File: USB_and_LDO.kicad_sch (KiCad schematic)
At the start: 12 parts, among them J2 USB_C_Receptacle_USB2.0_16P, U2 USBLC6-2SC6, U3 MCP1755S

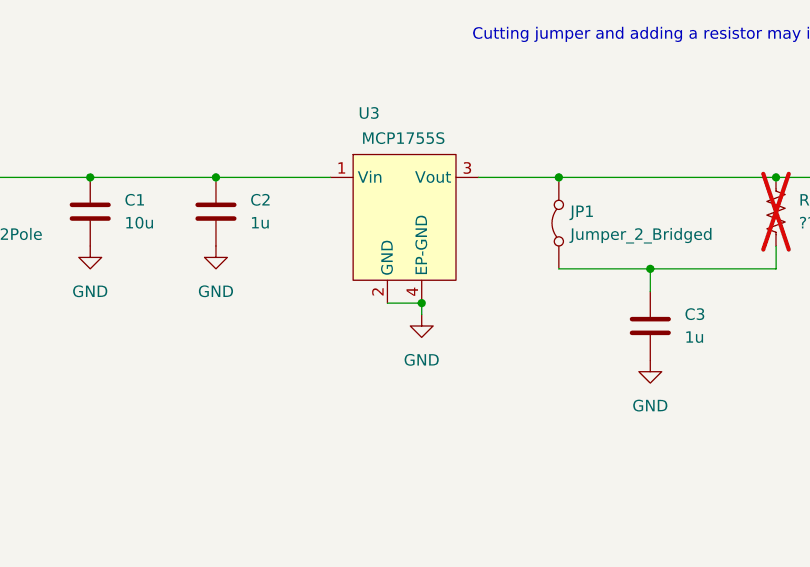
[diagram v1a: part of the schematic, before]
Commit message: Added all footprints
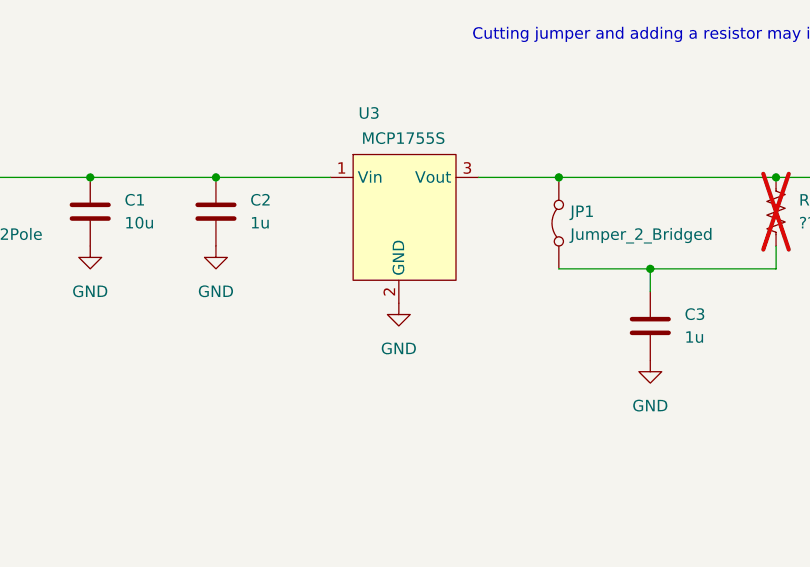
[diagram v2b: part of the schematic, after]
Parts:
- C1, C2, C3: footprint (none) -> Capacitor_SMD:C_1206_3216Metric_Pad1.33x1.80mm_HandSolder
- J2: footprint (none) -> Connector_USB:USB_C_Receptacle_GCT_USB4085
- JP1: footprint (none) -> Jumper:SolderJumper-2_P1.3mm_Bridged_RoundedPad1.0x1.5mm
- R1, R2, R3: footprint (none) -> Resistor_SMD:R_1206_3216Metric_Pad1.30x1.75mm_HandSolder
- TP1, TP2: footprint (none) -> TestPoint:TestPoint_2Pads_Pitch2.54mm_Drill0.8mm
- U3: footprint (none) -> Package_TO_SOT_SMD:SOT-223-3_TabPin2
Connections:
- net GND: no longer U3.4 (EP-GND)
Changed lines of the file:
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@@
-	)
-	(junction
-		(at 190.5 102.87)
-		(diameter 0)
-		(color 0 0 0 0)
 	)
 	(junction
@@
 	(wire
 		(pts
-			(xy 186.69 102.87) (xy 190.5 102.87)
-		)
-		(stroke
-			(width 0)
-			(type default)
-		)
-	)
-	(wire
-		(pts
-			(xy 190.5 102.87) (xy 190.5 104.14)
-		)
-		(stroke
-			(width 0)
-			(type default)
-		)
-	)
-	(wire
-		(pts
 			(xy 59.69 78.74) (xy 59.69 81.28)
 		)
@@
 	(symbol
 		(lib_id "power:GND")
-		(at 190.5 104.14 0)
+		(at 187.96 102.87 0)
 		(unit 1)
 		(exclude_from_sim no)
@@
 		(fields_autoplaced yes)
 		(property "Reference" "#PWR014"
-			(at 190.5 110.49 0)
+			(at 187.96 109.22 0)
 			(effects
 				(font
@@
 		)
 		(property "Value" "GND"
-			(at 190.5 109.22 0)
+			(at 187.96 107.95 0)
 			(effects
 				(font
@@
 		)
 		(property "Footprint" ""
-			(at 190.5 104.14 0)
+			(at 187.96 102.87 0)
 			(effects
 				(font
@@
 		)
 		(property "Datasheet" ""
-			(at 190.5 104.14 0)
+			(at 187.96 102.87 0)
 			(effects
 				(font
@@
 		)
 		(property "Description" "Power symbol creates a global label with name \"GND\" , ground"
-			(at 190.5 104.14 0)
+			(at 187.96 102.87 0)
 			(effects
 				(font
@@
 			)
 		)
-		(property "Footprint" ""
+		(property "Footprint" "Package_TO_SOT_SMD:SOT-223-3_TabPin2"
 			(at 187.96 92.71 0)
 			(effects
@@
 		(pin "2"
 		)
-		(pin "4"
-		)
 		(instances
 			(project "STM32F0-32pin-USBC"
@@
 			)
 		)
-		(property "Footprint" ""
+		(property "Footprint" "Resistor_SMD:R_1206_3216Metric_Pad1.30x1.75mm_HandSolder"
 			(at 50.546 133.604 90)
 			(effects
@@
 			)
 		)
-		(property "Footprint" ""
+		(property "Footprint" "Jumper:SolderJumper-2_P1.3mm_Bridged_RoundedPad1.0x1.5mm"
 			(at 205.74 93.98 0)
 			(effects
@@
 			)
 		)
-		(property "Footprint" ""
+		(property "Footprint" "TestPoint:TestPoint_2Pads_Pitch2.54mm_Drill0.8mm"
 			(at 132.08 93.98 0)
 			(effects
@@
 			)
 		)
-		(property "Footprint" ""
+		(property "Footprint" "Resistor_SMD:R_1206_3216Metric_Pad1.30x1.75mm_HandSolder"
 			(at 230.886 92.964 90)
 			(effects
@@
 			)
 		)
-		(property "Footprint" ""
+		(property "Footprint" "Resistor_SMD:R_1206_3216Metric_Pad1.30x1.75mm_HandSolder"
 			(at 35.306 133.604 90)
 			(effects
@@
 			)
 		)
-		(property "Footprint" ""
+		(property "Footprint" "Capacitor_SMD:C_1206_3216Metric_Pad1.33x1.80mm_HandSolder"
 			(at 168.6052 96.52 0)
 			(effects
@@
 			)
 		)
-		(property "Footprint" ""
+		(property "Footprint" "Capacitor_SMD:C_1206_3216Metric_Pad1.33x1.80mm_HandSolder"
 			(at 216.8652 109.22 0)
 			(effects
@@
 			)
 		)
-		(property "Footprint" ""
+		(property "Footprint" "TestPoint:TestPoint_2Pads_Pitch2.54mm_Drill0.8mm"
 			(at 241.3 93.98 0)
 			(effects
@@
 			)
 		)
-		(property "Footprint" ""
+		(property "Footprint" "Capacitor_SMD:C_1206_3216Metric_Pad1.33x1.80mm_HandSolder"
 			(at 154.6352 96.52 0)
 			(effects
@@
 			)
 		)
-		(property "Footprint" ""
+		(property "Footprint" "Connector_USB:USB_C_Receptacle_GCT_USB4085"
 			(at 48.26 81.28 0)
 			(effects

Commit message: finished part nubers in BOM
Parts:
- C1: MFR (none) -> Kemet; MFR Part No (none) -> C1206C106K4RACTU
- C2, C3: MFR (none) -> Kemet; MFR Part No (none) -> C1206C105K4RACTU
- J2: MFR (none) -> GCT; MFR Part No (none) -> USB4085-GF-A
- R1, R2: MFR (none) -> Vishay; MFR Part No (none) -> CRCW12065K10FKEA
- U2: MFR (none) -> STMicroelectronics; MFR Part No (none) -> USBLC6-2SC6
- U3: MFR (none) -> Microchip; MFR Part No (none) -> MCP1755S-3302E/DB
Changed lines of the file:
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@@
 			)
 		)
-		(property "MFR" ""
+		(property "MFR" "Microchip"
 			(at 187.96 92.71 0)
 			(effects
@@
 			)
 		)
-		(property "MFR Part No" ""
+		(property "MFR Part No" "MCP1755S-3302E/DB"
 			(at 187.96 92.71 0)
 			(effects
@@
 			)
 		)
-		(property "MFR" ""
+		(property "MFR" "STMicroelectronics"
 			(at 77.47 81.28 0)
 			(effects
@@
 			)
 		)
-		(property "MFR Part No" ""
+		(property "MFR Part No" "USBLC6-2SC6"
 			(at 77.47 81.28 0)
 			(effects
@@
 			)
 		)
-		(property "MFR" ""
+		(property "MFR" "Vishay"
 			(at 49.53 133.35 0)
 			(effects
@@
 			)
 		)
-		(property "MFR Part No" ""
+		(property "MFR Part No" "CRCW12065K10FKEA"
 			(at 49.53 133.35 0)
 			(effects
@@
 			)
 		)
-		(property "MFR" ""
+		(property "MFR" "Vishay"
 			(at 34.29 133.35 0)
 			(effects
@@
 			)
 		)
-		(property "MFR Part No" ""
+		(property "MFR Part No" "CRCW12065K10FKEA"
 			(at 34.29 133.35 0)
 			(effects
@@
 			)
 		)
-		(property "MFR" ""
+		(property "MFR" "Kemet"
 			(at 167.64 92.71 0)
 			(effects
@@
 			)
 		)
-		(property "MFR Part No" ""
+		(property "MFR Part No" "C1206C105K4RACTU"
 			(at 167.64 92.71 0)
 			(effects
@@
 			)
 		)
-		(property "MFR" ""
+		(property "MFR" "Kemet"
 			(at 215.9 105.41 0)
 			(effects
@@
 			)
 		)
-		(property "MFR Part No" ""
+		(property "MFR Part No" "C1206C105K4RACTU"
 			(at 215.9 105.41 0)
 			(effects
@@
 			)
 		)
-		(property "MFR" ""
+		(property "MFR" "Kemet"
 			(at 153.67 92.71 0)
 			(effects
@@
 			)
 		)
-		(property "MFR Part No" ""
+		(property "MFR Part No" "C1206C106K4RACTU"
 			(at 153.67 92.71 0)
 			(effects
@@
 			)
 		)
-		(property "MFR" ""
+		(property "MFR" "GCT"
 			(at 44.45 81.28 0)
 			(effects
@@
 			)
 		)
-		(property "MFR Part No" ""
+		(property "MFR Part No" "USB4085-GF-A"
 			(at 44.45 81.28 0)
 			(effects

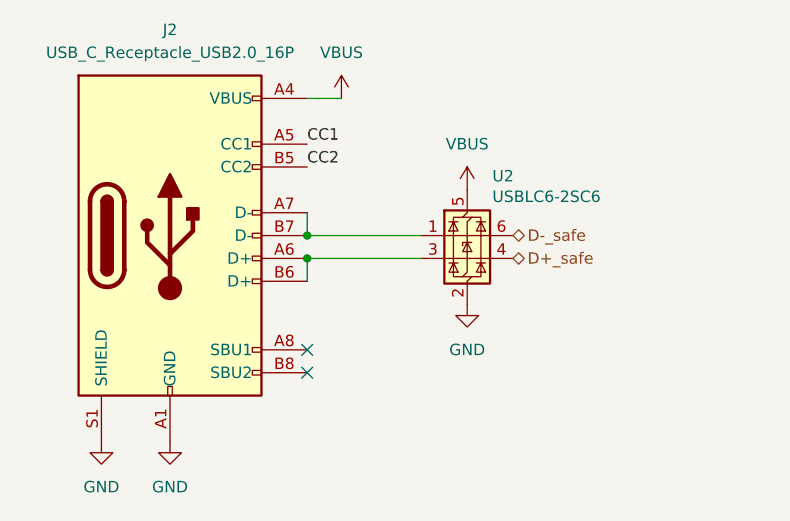
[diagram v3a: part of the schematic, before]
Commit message: preliminary footprint placement
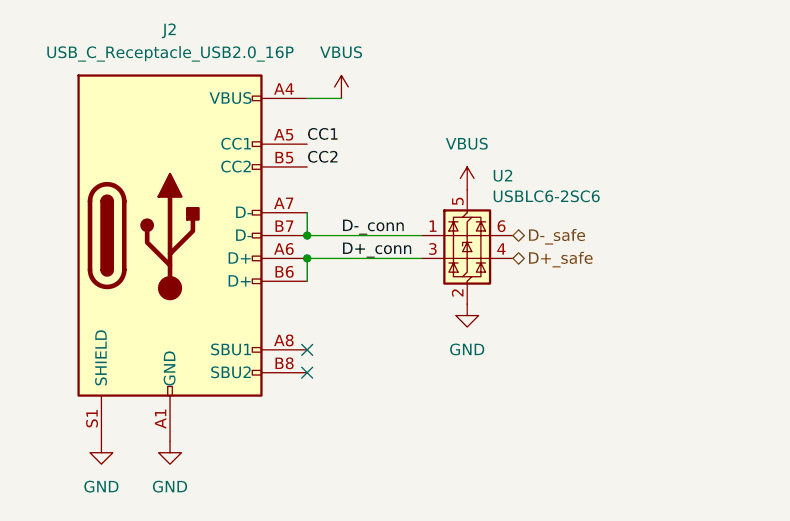
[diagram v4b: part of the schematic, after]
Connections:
- net D-_conn: now reaches J2.A7 (D-), J2.B7 (D-), U2.1 (I/O1)
- net D+_conn: now reaches J2.A6 (D+), J2.B6 (D+), U2.3 (I/O2)
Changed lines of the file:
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@@
+		)
+	)
+	(label "D+_conn"
+		(at 63.5 83.82 0)
+		(fields_autoplaced yes)
+		(effects
+			(font
+				(size 1.27 1.27)
+			)
+			(justify left bottom)
+		)
+	)
+	(label "D-_conn"
+		(at 63.5 81.28 0)
+		(fields_autoplaced yes)
+		(effects
+			(font
+				(size 1.27 1.27)
+			)
+			(justify left bottom)
 		)
 	)

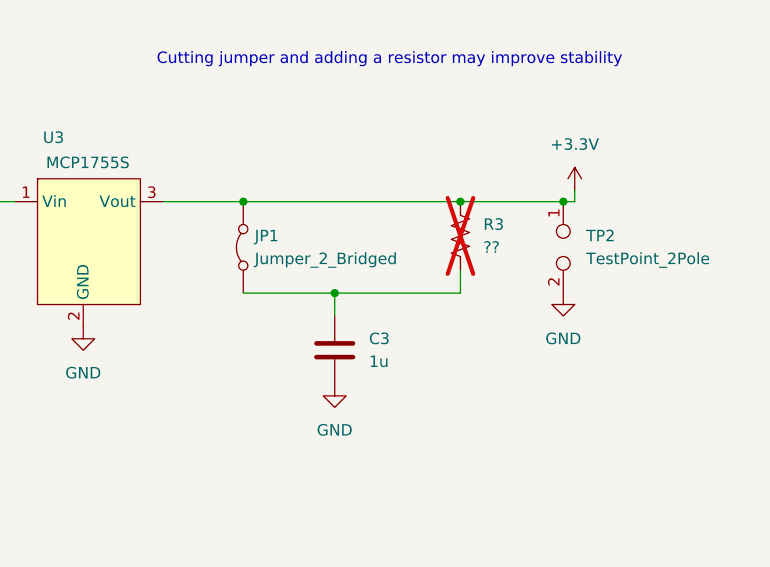
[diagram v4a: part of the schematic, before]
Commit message: everything routed but ground
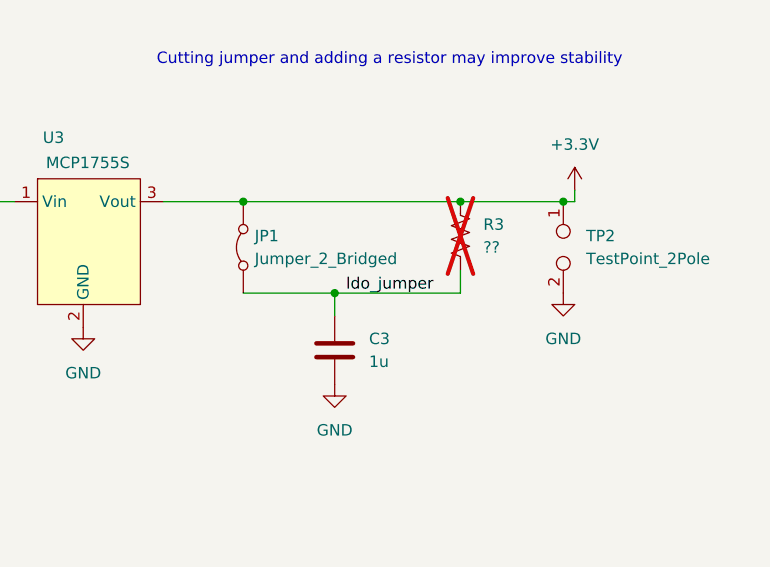
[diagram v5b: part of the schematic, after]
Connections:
- net ldo_jumper: now reaches C3.1, JP1.1 (A), R3.2
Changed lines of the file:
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@@
+		)
+	)
+	(label "ldo_jumper"
+		(at 217.17 99.06 0)
+		(fields_autoplaced yes)
+		(effects
+			(font
+				(size 1.27 1.27)
+			)
+			(justify left bottom)
 		)
 	)

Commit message: switched to small pad size usb conn and drew board edge
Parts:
- J2: footprint Connector_USB:USB_C_Receptacle_GCT_USB4085 -> AAAA_HugonLib:USB_C_Receptacle_GCT_USB4085_Reduced_Pad_Size
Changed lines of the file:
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@@
 			)
 		)
-		(property "Footprint" "Connector_USB:USB_C_Receptacle_GCT_USB4085"
+		(property "Footprint" "AAAA_HugonLib:USB_C_Receptacle_GCT_USB4085_Reduced_Pad_Size"
 			(at 48.26 81.28 0)
 			(effects

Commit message: update all R's and all C's but 10u to 0805 from 1206
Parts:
- C2, C3: footprint Capacitor_SMD:C_1206_3216Metric_Pad1.33x1.80mm_HandSolder -> Capacitor_SMD:C_0805_2012Metric_Pad1.18x1.45mm_HandSolder; MFR Part No C1206C105K4RACTU -> C0805C105K4RACTU
- R1, R2: footprint Resistor_SMD:R_1206_3216Metric_Pad1.30x1.75mm_HandSolder -> Resistor_SMD:R_0805_2012Metric_Pad1.20x1.40mm_HandSolder; MFR Part No CRCW12065K10FKEA -> CRCW08055K10FKEA
- R3: footprint Resistor_SMD:R_1206_3216Metric_Pad1.30x1.75mm_HandSolder -> Resistor_SMD:R_0805_2012Metric_Pad1.20x1.40mm_HandSolder
- U3: symbol AAAA_HugonLib:MCP1755S-XX02/DB -> AAAA_HugonLib:MCP1755S-XX02E/DB; MFR Part No MCP1755S-3302E/DB -> MCP1755S-XX02E/DB
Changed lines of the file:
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@@
 	)
 	(symbol
-		(lib_id "AAAA_HugonLib:MCP1755S-XX02/DB")
+		(lib_id "AAAA_HugonLib:MCP1755S-XX02E/DB")
 		(at 187.96 92.71 0)
 		(unit 1)
@@
 			)
 		)
-		(property "MFR Part No" "MCP1755S-3302E/DB"
+		(property "MFR Part No" "MCP1755S-XX02E/DB"
 			(at 187.96 92.71 0)
 			(effects
@@
 			)
 		)
-		(property "Footprint" "Resistor_SMD:R_1206_3216Metric_Pad1.30x1.75mm_HandSolder"
+		(property "Footprint" "Resistor_SMD:R_0805_2012Metric_Pad1.20x1.40mm_HandSolder"
 			(at 50.546 133.604 90)
 			(effects
@@
 			)
 		)
-		(property "MFR Part No" "CRCW12065K10FKEA"
+		(property "MFR Part No" "CRCW08055K10FKEA"
 			(at 49.53 133.35 0)
 			(effects
@@
 			)
 		)
-		(property "Footprint" "Resistor_SMD:R_1206_3216Metric_Pad1.30x1.75mm_HandSolder"
+		(property "Footprint" "Resistor_SMD:R_0805_2012Metric_Pad1.20x1.40mm_HandSolder"
 			(at 230.886 92.964 90)
 			(effects
@@
 			)
 		)
-		(property "Footprint" "Resistor_SMD:R_1206_3216Metric_Pad1.30x1.75mm_HandSolder"
+		(property "Footprint" "Resistor_SMD:R_0805_2012Metric_Pad1.20x1.40mm_HandSolder"
 			(at 35.306 133.604 90)
 			(effects
@@
 			)
 		)
-		(property "MFR Part No" "CRCW12065K10FKEA"
+		(property "MFR Part No" "CRCW08055K10FKEA"
 			(at 34.29 133.35 0)
 			(effects
@@
 			)
 		)
-		(property "Footprint" "Capacitor_SMD:C_1206_3216Metric_Pad1.33x1.80mm_HandSolder"
+		(property "Footprint" "Capacitor_SMD:C_0805_2012Metric_Pad1.18x1.45mm_HandSolder"
 			(at 168.6052 96.52 0)
 			(effects
@@
 			)
 		)
-		(property "MFR Part No" "C1206C105K4RACTU"
+		(property "MFR Part No" "C0805C105K4RACTU"
 			(at 167.64 92.71 0)
 			(effects
@@
 			)
 		)
-		(property "Footprint" "Capacitor_SMD:C_1206_3216Metric_Pad1.33x1.80mm_HandSolder"
+		(property "Footprint" "Capacitor_SMD:C_0805_2012Metric_Pad1.18x1.45mm_HandSolder"
 			(at 216.8652 109.22 0)
 			(effects
@@
 			)
 		)
-		(property "MFR Part No" "C1206C105K4RACTU"
+		(property "MFR Part No" "C0805C105K4RACTU"
 			(at 215.9 105.41 0)
 			(effects

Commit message: Changed to 0805 for most Rs and C's
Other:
- company: (none) -> HugonLabs
- title: (none) -> STM32F0 32 Pin USB-C
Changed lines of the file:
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@@
 	(generator "eeschema")
 	(generator_version "8.0")
-	(paper "A4")
+	(paper "USLetter")
+	(title_block
+		(title "STM32F0 32 Pin USB-C")
+		(date "2024-04-18")
+		(rev "1.0")
+		(company "HugonLabs")
+	)
 	(junction
 		(at 132.08 88.9)
